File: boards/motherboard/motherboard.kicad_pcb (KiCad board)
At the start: 2 copper layers, 214.4 x 64 mm, 50 parts, among them CN1 CONN_01X02, CN2 CONN_01X02, CN3 CONN_01X02, CN4 CONN_01X02, CN5 CONN_01X02, J1 RJ45, J2 RJ45, J3 RJ45, J4 RJ45, J5 RJ45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

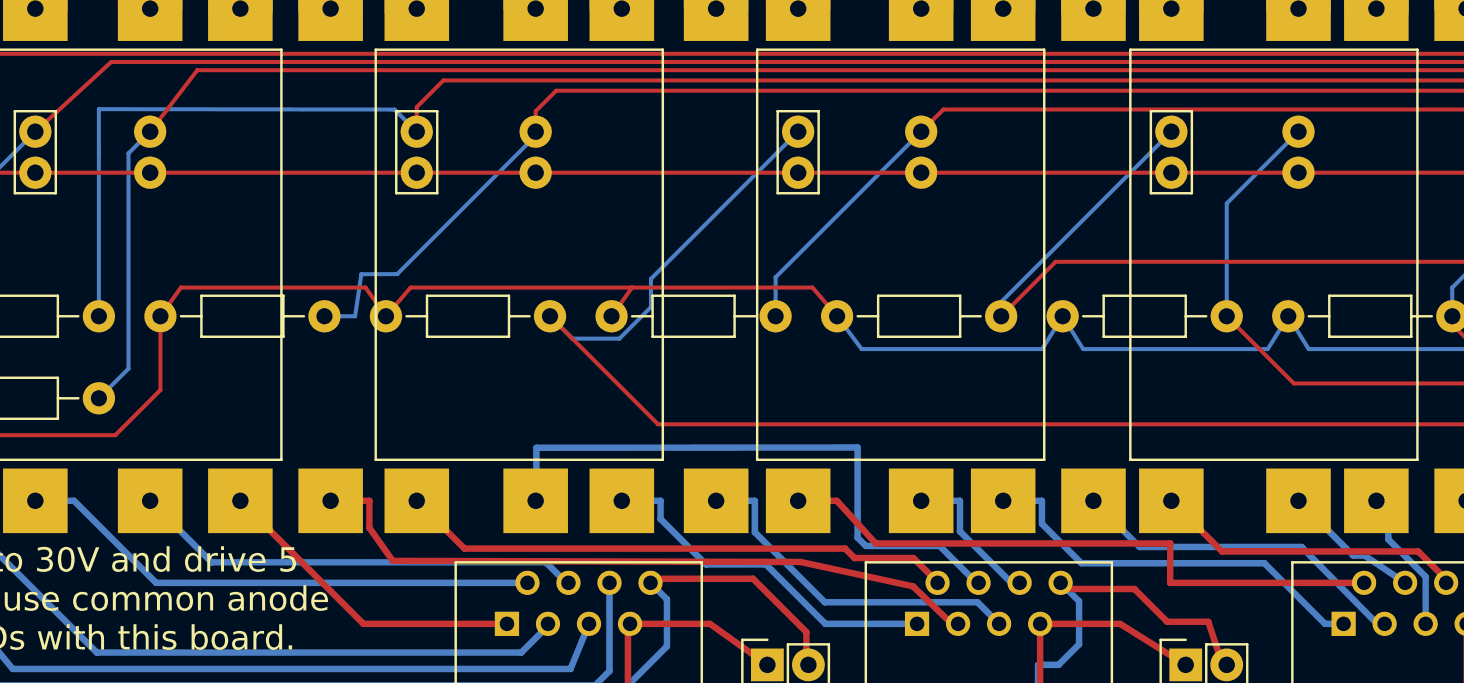
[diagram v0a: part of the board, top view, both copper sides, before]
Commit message: minor track changes
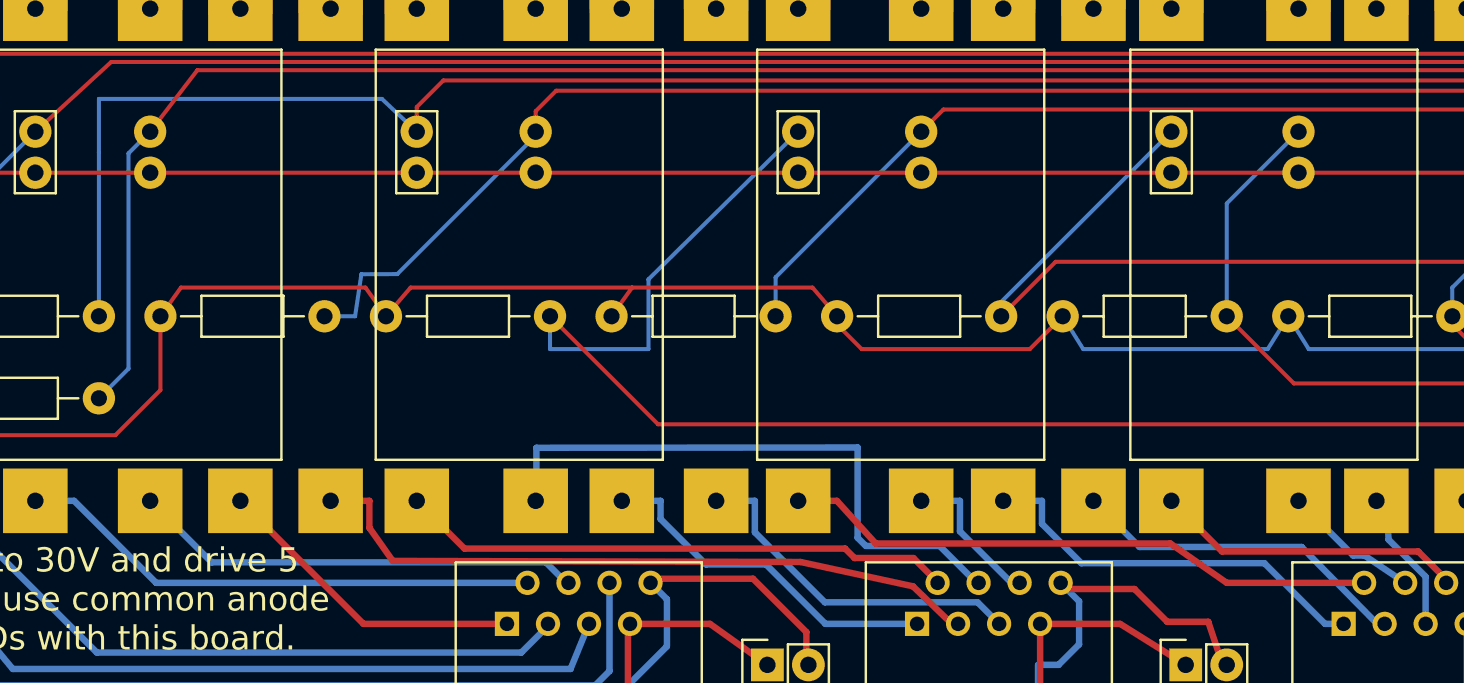
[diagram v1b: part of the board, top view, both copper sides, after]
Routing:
- net /led6: track 163.9 -> 167.1 mm
- net Net-(350ma7-Pad3): track 38.7 -> 37.0 mm
- net /led9: track 193.7 -> 194.6 mm
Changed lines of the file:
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@@
     (thickness 1.6)
     (drawings 40)
-    (tracks 524)
+    (tracks 525)
     (zones 0)
     (modules 50)
@@
     (pad_to_mask_clearance 0.2)
     (aux_axis_origin 0 0)
-    (visible_elements FFFFFF7F)
+    (visible_elements FFFFF77F)
     (pcbplotparams
       (layerselection 0x010f0_80000001)
-      (usegerberextensions false)
+      (usegerberextensions true)
       (excludeedgelayer true)
       (linewidth 0.100000)
@@
       (padsonsilk false)
       (subtractmaskfromsilk false)
-      (outputformat 3)
+      (outputformat 1)
       (mirror false)
       (drillshape 0)
       (scaleselection 1)
-      (outputdirectory dxf/))
+      (outputdirectory gerber))
   )
   (net 0 "")
@@
   (segment (start 188.214 78.74) (end 188.214 76.835) (width 0.25) (layer B.Cu) (net 20))
   (segment (start 188.214 76.835) (end 197.739 67.31) (width 0.25) (layer B.Cu) (net 20))
-  (segment (start 142.8115 92.8116) (end 142.7988 95.25) (width 0.4) (layer F.Cu) (net 21))
-  (segment (start 142.7988 95.25) (end 154.813 95.25) (width 0.4) (layer F.Cu) (net 21))
+  (segment (start 142.8115 92.8116) (end 146.304 95.25) (width 0.4) (layer F.Cu) (net 21))
+  (segment (start 146.304 95.25) (end 154.813 95.25) (width 0.4) (layer F.Cu) (net 21))
   (segment (start 124.5616 92.8116) (end 142.8115 92.8116) (width 0.4) (layer F.Cu) (net 21))
   (segment (start 122.1613 90.17) (end 124.5616 92.8116) (width 0.4) (layer F.Cu) (net 21))
@@
   (segment (start 134.8613 91.5952) (end 137.3015 94.0354) (width 0.4) (layer B.Cu) (net 22))
   (segment (start 134.8613 90.17) (end 134.8613 91.5952) (width 0.4) (layer B.Cu) (net 22))
-  (segment (start 105.7781 80.1241) (end 104.394 78.74) (width 0.25) (layer B.Cu) (net 23))
-  (segment (start 108.6944 80.1241) (end 105.7781 80.1241) (width 0.25) (layer B.Cu) (net 23))
-  (segment (start 110.6446 78.1739) (end 108.6944 80.1241) (width 0.25) (layer B.Cu) (net 23))
-  (segment (start 110.6446 76.4264) (end 110.6446 78.1739) (width 0.25) (layer B.Cu) (net 23))
-  (segment (start 119.761 67.31) (end 110.6446 76.4264) (width 0.25) (layer B.Cu) (net 23))
+  (segment (start 104.394 80.772) (end 104.394 78.74) (width 0.25) (layer B.Cu) (net 23))
+  (segment (start 110.49 80.772) (end 104.394 80.772) (width 0.25) (layer B.Cu) (net 23))
+  (segment (start 110.49 76.454) (end 110.49 80.772) (width 0.25) (layer B.Cu) (net 23))
+  (segment (start 110.49 76.454) (end 110.49 76.454) (width 0.25) (layer B.Cu) (net 23))
+  (segment (start 119.761 67.31) (end 110.49 76.454) (width 0.25) (layer B.Cu) (net 23))
   (segment (start 111.0848 85.4308) (end 104.394 78.74) (width 0.25) (layer F.Cu) (net 23))
   (segment (start 241.7212 85.4308) (end 111.0848 85.4308) (width 0.25) (layer F.Cu) (net 23))
@@
   (segment (start 97.79 64.135) (end 96.139 65.786) (width 0.25) (layer F.Cu) (net 31))
   (segment (start 76.454 68.608) (end 76.454 78.74) (width 0.25) (layer B.Cu) (net 31))
-  (segment (start 76.454 65.913) (end 76.454 68.608) (width 0.25) (layer B.Cu) (net 31))
-  (segment (start 94.7686 65.9396) (end 76.454 65.913) (width 0.25) (layer B.Cu) (net 31))
-  (segment (start 96.139 67.31) (end 94.7686 65.9396) (width 0.25) (layer B.Cu) (net 31))
+  (segment (start 76.454 65.278) (end 76.454 68.608) (width 0.25) (layer B.Cu) (net 31))
+  (segment (start 93.98 65.278) (end 76.454 65.278) (width 0.25) (layer B.Cu) (net 31))
+  (segment (start 96.139 67.31) (end 93.98 65.278) (width 0.25) (layer B.Cu) (net 31))
   (segment (start 103.549537 90.125463) (end 103.549537 86.884895) (width 0.4) (layer B.Cu) (net 32))
   (segment (start 128.524 92.964) (end 123.952 92.964) (width 0.4) (layer B.Cu) (net 32))
@@
   (segment (start 241.554 57.658) (end 237.2232 57.658) (width 0.25) (layer F.Cu) (net 46))
   (segment (start 242.824 56.388) (end 241.554 57.658) (width 0.25) (layer F.Cu) (net 46))
+  (segment (start 136.144 78.74) (end 134.112 80.772) (width 0.25) (layer F.Cu) (net 47) (status 400000))
+  (segment (start 123.698 80.772) (end 122.174 79.248) (width 0.25) (layer F.Cu) (net 47) (status 800000))
+  (segment (start 134.112 80.772) (end 123.698 80.772) (width 0.25) (layer F.Cu) (net 47))
+  (segment (start 122.174 79.248) (end 122.174 78.74) (width 0.25) (layer F.Cu) (net 47) (status C00000))
   (segment (start 66.294 83.82) (end 66.294 78.74) (width 0.25) (layer F.Cu) (net 47))
   (segment (start 51.054 83.82) (end 51.054 78.74) (width 0.25) (layer F.Cu) (net 47))
@@
   (segment (start 95.758 76.962) (end 94.234 78.74) (width 0.25) (layer F.Cu) (net 47))
   (segment (start 109.474 76.962) (end 95.758 76.962) (width 0.25) (layer F.Cu) (net 47))
-  (segment (start 123.698 80.772) (end 122.174 78.74) (width 0.25) (layer B.Cu) (net 47))
-  (segment (start 134.874 80.772) (end 123.698 80.772) (width 0.25) (layer B.Cu) (net 47))
-  (segment (start 136.144 78.74) (end 134.874 80.772) (width 0.25) (layer B.Cu) (net 47))
   (segment (start 148.844 80.772) (end 150.114 78.74) (width 0.25) (layer B.Cu) (net 47))
   (segment (start 137.414 80.772) (end 148.844 80.772) (width 0.25) (layer B.Cu) (net 47))

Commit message: minor tweaks
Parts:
- moved BLK3 4.75 mm to (47.5, 104.6), turned to 270 degrees
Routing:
- net Net-(350ma3-Pad3): track 10.1 -> 12.2 mm
- net GND: track 291.7 -> 289.7 mm
- net Net-(350ma12-Pad3): track 9.31 -> 8.06 mm
- net Net-(350ma11-Pad4): track 42.7 -> 41.5 mm
- net Net-(350ma7-Pad4): track 25.1 -> 24.2 mm
- net Net-(350ma15-Pad4): track 53.2 -> 52.4 mm
- net Net-(350ma8-Pad4): track 21.2 -> 21.9 mm
- net Net-(350ma10-Pad4): track 22.1 -> 21.4 mm
- net /led14: track 217.1 -> 217.6 mm
